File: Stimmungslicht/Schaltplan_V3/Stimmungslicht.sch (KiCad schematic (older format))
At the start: 19 parts, among them IC1 STM32G031J6M6, J1 Conn_01x01, J2 Conn_01x04_Male, U1 HU2032-LF, U101 Touch_Sens_Pad, U102 Touch_Sens_Pad, U103 Touch_Sens_Pad, U104 Touch_Sens_Pad

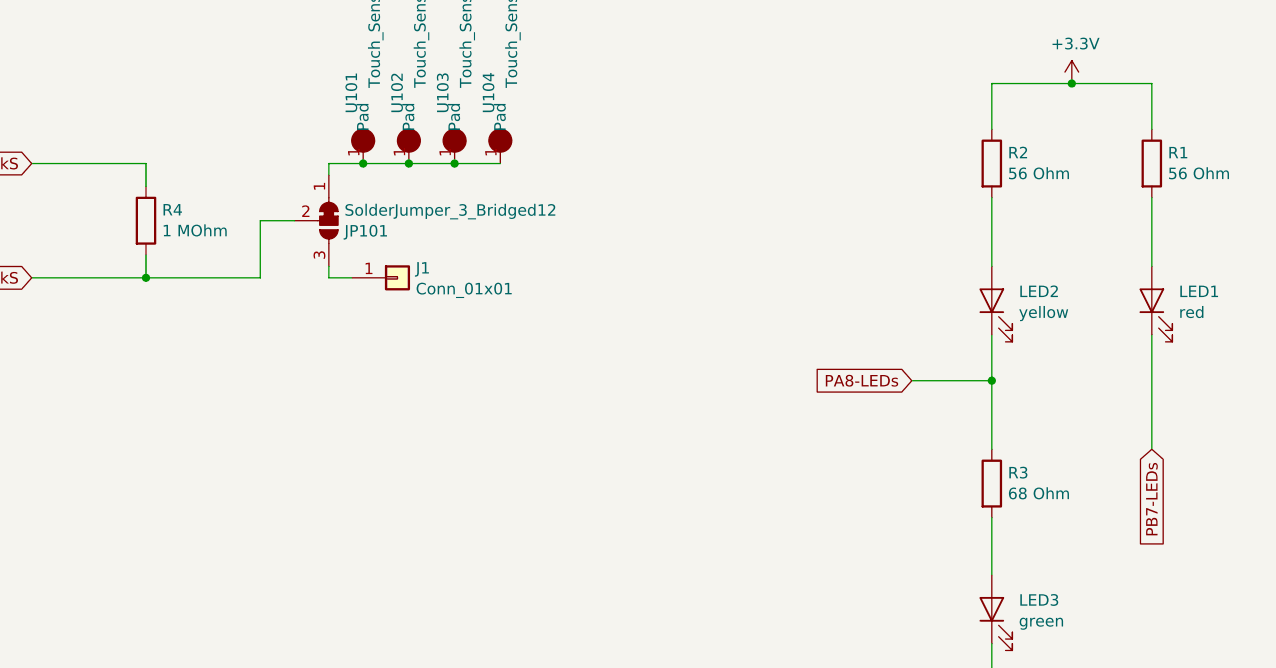
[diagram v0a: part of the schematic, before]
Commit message: Widerstandswerte korrekt
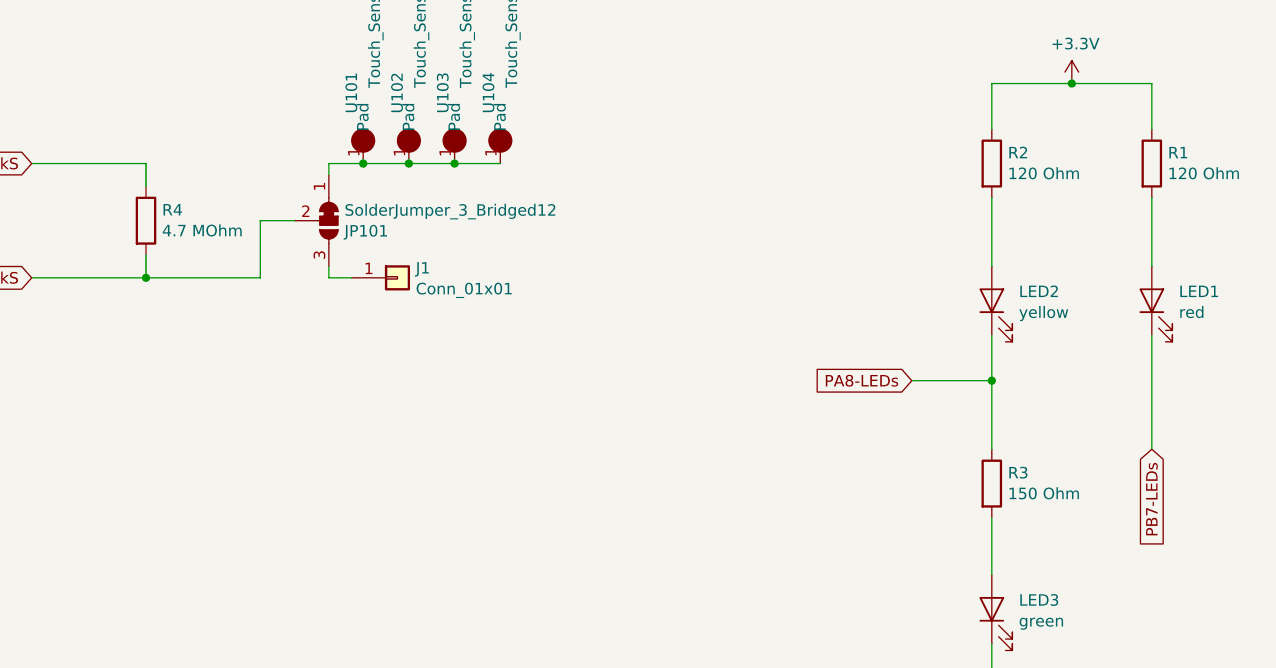
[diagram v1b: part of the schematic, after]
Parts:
- R1, R2: value 56 Ohm -> 120 Ohm
- R3: value 68 Ohm -> 150 Ohm
- R4: value 1 MOhm -> 4.7 MOhm
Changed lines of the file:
@@
 P 8400 3100
 F 0 "R3" H 8470 3146 50  0000 L CNN
-F 1 "68 Ohm" H 8470 3055 50  0000 L CNN
+F 1 "150 Ohm" H 8470 3055 50  0000 L CNN
 F 2 "Resistor_SMD:R_0603_1608Metric_Pad1.05x0.95mm_HandSolder" V 8330 3100 50  0001 C CNN
 F 3 "~" H 8400 3100 50  0001 C CNN
@@
 P 8400 1700
 F 0 "R2" H 8470 1746 50  0000 L CNN
-F 1 "56 Ohm" H 8470 1655 50  0000 L CNN
+F 1 "120 Ohm" H 8470 1655 50  0000 L CNN
 F 2 "Resistor_SMD:R_0603_1608Metric_Pad1.05x0.95mm_HandSolder" V 8330 1700 50  0001 C CNN
 F 3 "~" H 8400 1700 50  0001 C CNN
@@
 P 9100 1700
 F 0 "R1" H 9170 1746 50  0000 L CNN
-F 1 "56 Ohm" H 9170 1655 50  0000 L CNN
+F 1 "120 Ohm" H 9170 1655 50  0000 L CNN
 F 2 "Resistor_SMD:R_0603_1608Metric_Pad1.05x0.95mm_HandSolder" V 9030 1700 50  0001 C CNN
 F 3 "~" H 9100 1700 50  0001 C CNN
@@
 P 4700 1950
 F 0 "R4" H 4770 1996 50  0000 L CNN
-F 1 "1 MOhm" H 4770 1905 50  0000 L CNN
+F 1 "4.7 MOhm" H 4770 1905 50  0000 L CNN
 F 2 "Resistor_SMD:R_0603_1608Metric_Pad1.05x0.95mm_HandSolder" V 4630 1950 50  0001 C CNN
 F 3 "~" H 4700 1950 50  0001 C CNN
